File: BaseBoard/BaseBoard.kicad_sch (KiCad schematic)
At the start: 22 parts, among them J1 OHIS RJ45, J2 Radio Board, J3 Dynamic/Electret, J6 Speaker Input Config

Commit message: Happy with BaseBoard and Icom-RJ45. Working on Icom-GX16 #1
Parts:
- added G2: Board_Artwork, OHIS:Logo_OHIS_Medium, symbol Smitty:Board_Artwork
- G1: footprint OHIS:Logo_OHIS_Small -> OHIS:Logo_OHIS_Medium
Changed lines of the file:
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@@
+	)
+	(symbol
+		(lib_id "Smitty:Board_Artwork")
+		(at 83.82 168.91 0)
+		(unit 1)
+		(exclude_from_sim no)
+		(in_bom no)
+		(on_board yes)
+		(dnp no)
+		(fields_autoplaced yes)
+		(property "Reference" "G2"
+			(at 87.63 169.4179 0)
+			(effects
+				(font
+					(size 1.27 1.27)
+				)
+				(justify left)
+			)
+		)
+		(property "Value" "Board_Artwork"
+			(at 87.63 171.9579 0)
+			(effects
+				(font
+					(size 1.27 1.27)
+				)
+				(justify left)
+			)
+		)
+		(property "Footprint" "OHIS:Logo_OHIS_Medium"
+			(at 83.82 168.91 0)
+			(effects
+				(font
+					(size 1.27 1.27)
+				)
+			)
+		)
+		(property "Datasheet" ""
+			(at 83.82 168.91 0)
+			(effects
+				(font
+					(size 1.27 1.27)
+				)
+				(hide yes)
+			)
+		)
+		(property "Description" ""
+			(at 83.82 168.91 0)
+			(effects
+				(font
+					(size 1.27 1.27)
+				)
+				(hide yes)
+			)
+		)
+		(instances
+			(project "BaseBoard"
+				(path "/6a3924fa-c381-477c-bc5e-4effe098c460"
+					(reference "G2")
+					(unit 1)
+				)
+			)
+		)
 	)
 	(symbol
@@
 			)
 		)
-		(property "Footprint" "OHIS:Logo_OHIS_Small"
+		(property "Footprint" "OHIS:Logo_OHIS_Medium"
 			(at 83.82 161.29 0)
 			(effects

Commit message: Updated BOM parts, among other things. Sorry, it's been a while. #1
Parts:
- removed RV1: 1k, Potentiometer_THT:Potentiometer_Piher_PT-6-H_Horizontal, symbol Device:R_Potentiometer
- added BOM1, BOM13, BOM17, BOM9: M3 6mm SS screw, Libraries:BOM_Item, symbol smitty:BOM_Item
- added BOM10, BOM14, BOM18, BOM3: M3 14mm brass standoff, Libraries:BOM_Item, symbol smitty:BOM_Item
- added BOM11, BOM15, BOM19, BOM7: M3 3mm ABS standoff, Libraries:BOM_Item, symbol smitty:BOM_Item
- added BOM12, BOM16, BOM6, BOM8: M3 10mm SS screw, Libraries:BOM_Item, symbol smitty:BOM_Item
- added BOM2: Top Board, Libraries:BOM_Item, symbol smitty:BOM_Item
- added BOM20, BOM21, BOM22, BOM23, BOM24: .1" Jumper, Libraries:BOM_Item, symbol smitty:BOM_Item
- added BOM4: Main Board, Libraries:BOM_Item, symbol smitty:BOM_Item
- added BOM5: Bottom Board, Libraries:BOM_Item, symbol smitty:BOM_Item
- added RV2: 1k, Potentiometer_THT:Potentiometer_Piher_PT-6-H_Horizontal, symbol Device:R_Potentiometer_Small
- C1, C2: Link (none) -> https://www.mouser.com/ProductDetail/TDK/FG28X5R1E106MRT06?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; Manufacturer (none) -> TDK; Part Number (none) -> FG28X5R1E106MRT06; Z0 Buy in Qty (none) -> 200; Z1 Cost to buy (none) -> =32.40
- C3, C4, R11, R12, R5, R7: now not fitted; now left out of the parts list
- J1: Link (none) -> https://www.mouser.com/ProductDetail/523-RJHSE-5380; Manufacturer (none) -> Amphenol; Part Number (none) -> RJHSE-5381; Z0 Buy in Qty (none) -> 120; Z1 Cost to buy (none) -> =127.20; Z2 Cost per part (none) -> =IFERROR(OFFSET(INDIRECT(CELL("Address")), 0, -1)/OFFSET(IN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; Z3 Cost per Qty (none) -> =OFFSET(INDIRECT(CELL("Address")), 0, -1)*INDIRECT(ADDRESS(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
- J3, J6: Link (none) -> https://www.ebay.com/itm/181918596973; Manufacturer (none) -> Generic; Part Number (none) -> .1" 3x40 right angle 2.54mm Pin Header; Z0 Buy in Qty (none) -> 40; Z1 Cost to buy (none) -> 2.49; Z2 Cost per part (none) -> =IFERROR(OFFSET(INDIRECT(CELL("Address")), 0, -1)/OFFSET(IN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; Z3 Cost per Qty (none) -> =OFFSET(INDIRECT(CELL("Address")), 0, -1)*INDIRECT(ADDRESS(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
- R1: Link (none) -> https://www.mouser.com/ProductDetail/YAGEO/CFR-12JB-52-1K?q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; Manufacturer (none) -> YAGEO; Part Number (none) -> CFR-12JB-52-1K; Z0 Buy in Qty (none) -> 100; Z1 Cost to buy (none) -> 2.80; Z2 Cost per part (none) -> =IFERROR(OFFSET(INDIRECT(CELL("Address")), 0, -1)/OFFSET(IN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; Z3 Cost per Qty (none) -> =OFFSET(INDIRECT(CELL("Address")), 0, -1)*INDIRECT(ADDRESS(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
- R4: Link (none) -> https://www.mouser.com/ProductDetail/YAGEO/CFR-12JB-52-6K2?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; Manufacturer (none) -> YAGEO; Part Number (none) -> CFR-12JB-52-6K2; Z0 Buy in Qty (none) -> 100; Z1 Cost to buy (none) -> 1.90
- R6, R8: Link (none) -> https://www.mouser.com/ProductDetail/YAGEO/CFR-12JB-52-100R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; Manufacturer (none) -> YAGEO; Part Number (none) -> CFR-12JB-52-100R; Z0 Buy in Qty (none) -> 100; Z1 Cost to buy (none) -> 2.80; Z2 Cost per part (none) -> =IFERROR(OFFSET(INDIRECT(CELL("Address")), 0, -1)/OFFSET(IN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; Z3 Cost per Qty (none) -> =OFFSET(INDIRECT(CELL("Address")), 0, -1)*INDIRECT(ADDRESS(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
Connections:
- net Radio Mic Gnd: now also RV2.1
- net at C2.1, C4.1: now also RV2.2
- net at C1.1, C3.1: now also RV2.3
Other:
- note added: "BOM: 1x 5381 RF45 with LEDs 1x 2x2 pin header right angle 1x 2x4 pin header right angle 2x 10uF 1x 6.2k resistor 1x 1k resistor 2x 100R resistors 1x 1k potentiometer"
- moved on the sheet: G1, G2

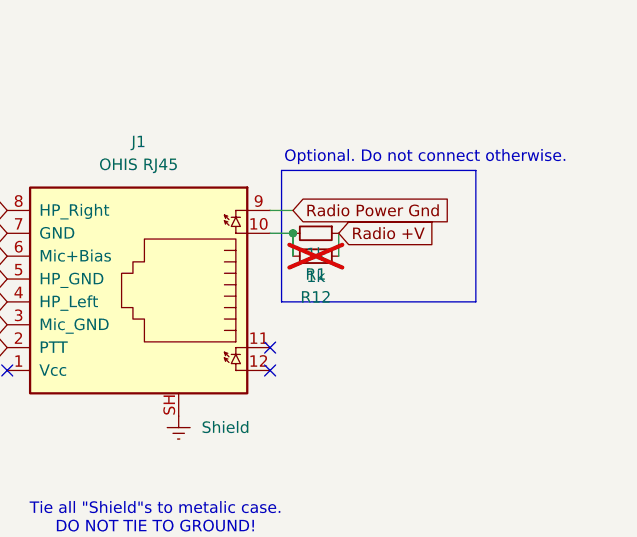
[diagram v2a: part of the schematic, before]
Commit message: Added an Interactive BOM for the Base Board assembly.
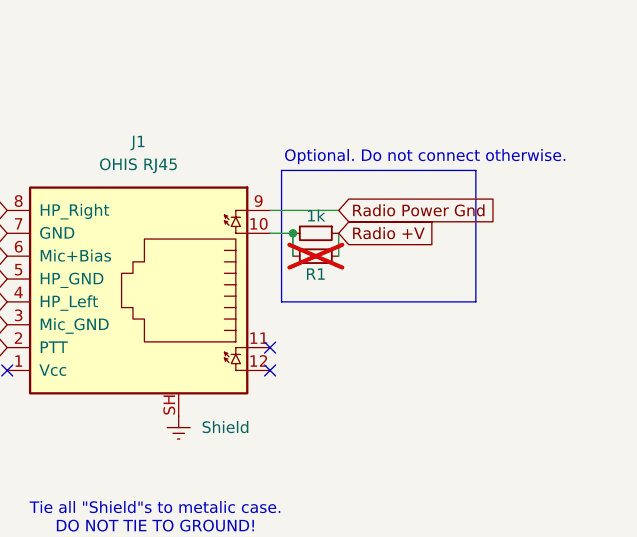
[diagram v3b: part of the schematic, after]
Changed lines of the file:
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@@
 (kicad_sch
-	(version 20231120)
+	(version 20250114)
 	(generator "eeschema")
-	(generator_version "8.0")
+	(generator_version "9.0")
 	(paper "A4")
+	(rectangle
+		(start 242.57 34.925)
+		(end 264.16 49.53)
+		(stroke
+			(width 0)
+			(type default)
+		)
+		(fill
+			(type none)
+		)
+	)
+	(text "Stereo Source"
+		(exclude_from_sim no)
+		(at 148.082 97.79 0)
+		(effects
+			(font
+				(size 1.27 1.27)
+			)
+		)
+	)
+	(text "OHIS Side: Electret Mic\nBias voltage."
+		(exclude_from_sim no)
+		(at 151.638 26.67 0)
+		(effects
+			(font
+				(size 1.27 1.27)
+			)
+		)
+	)
+	(text "Mono Source"
+		(exclude_from_sim no)
+		(at 147.574 100.33 0)
+		(effects
+			(font
+				(size 1.27 1.27)
+			)
+		)
+	)
+	(text "Radio Side: Dynamic Mic.\n20dB pad, DC block."
+		(exclude_from_sim no)
+		(at 122.682 33.274 0)
+		(effects
+			(font
+				(size 1.27 1.27)
+			)
+		)
+	)
+	(text "Tie all \"Shield\"s to metalic case.\nDO NOT TIE TO GROUND!"
+		(exclude_from_sim no)
+		(at 228.6 73.66 0)
+		(effects
+			(font
+				(size 1.27 1.27)
+			)
+		)
+	)
+	(text "1k*10uF=16Hz\n600*10uF=26Hz"
+		(exclude_from_sim no)
+		(at 131.572 20.574 0)
+		(effects
+			(font
+				(size 1.27 1.27)
+			)
+		)
+	)
+	(text "BOM:\n1x 5381 RF45 with LEDs\n1x 2x2 pin header right angle\n1x 2x4 pin header right angle\n2x 10uF\n1x 6.2k resistor\n1x 1k resistor\n2x 100R resistors\n1x 1k potentiometer\n"
+		(exclude_from_sim no)
+		(at 44.45 35.56 0)
+		(effects
+			(font
+				(size 1.27 1.27)
+			)
+			(justify left)
+		)
+	)
+	(text "Jumper: Headphone\nNo Jumper: Speaker"
+		(exclude_from_sim no)
+		(at 151.13 104.394 0)
+		(effects
+			(font
+				(size 1.27 1.27)
+			)
+		)
+	)
+	(text "Optional. Do not connect otherwise."
+		(exclude_from_sim no)
+		(at 258.572 33.528 0)
+		(effects
+			(font
+				(size 1.27 1.27)
+			)
+		)
+	)
 	(junction
 		(at 116.84 44.45)
@@
 	(wire
 		(pts
-			(xy 243.84 39.37) (xy 241.3 39.37)
+			(xy 248.92 39.37) (xy 241.3 39.37)
 		)
 		(stroke
@@
 		)
 	)
-	(rectangle
-		(start 242.57 34.925)
-		(end 264.16 49.53)
-		(stroke
-			(width 0)
-			(type default)
-		)
-		(fill
-			(type none)
-		)
-	)
-	(text "Stereo Source"
-		(exclude_from_sim no)
-		(at 148.082 97.79 0)
-		(effects
-			(font
-				(size 1.27 1.27)
-			)
-		)
-	)
-	(text "OHIS Side: Electret Mic\nBias voltage."
-		(exclude_from_sim no)
-		(at 151.638 26.67 0)
-		(effects
-			(font
-				(size 1.27 1.27)
-			)
-		)
-	)
-	(text "Mono Source"
-		(exclude_from_sim no)
-		(at 147.574 100.33 0)
-		(effects
-			(font
-				(size 1.27 1.27)
-			)
-		)
-	)
-	(text "Radio Side: Dynamic Mic.\n20dB pad, DC block."
-		(exclude_from_sim no)
-		(at 122.682 33.274 0)
-		(effects
-			(font
-				(size 1.27 1.27)
-			)
-		)
-	)
-	(text "Tie all \"Shield\"s to metalic case.\nDO NOT TIE TO GROUND!"
-		(exclude_from_sim no)
-		(at 228.6 73.66 0)
-		(effects
-			(font
-				(size 1.27 1.27)
-			)
-		)
-	)
-	(text "1k*10uF=16Hz\n600*10uF=26Hz"
-		(exclude_from_sim no)
-		(at 131.572 20.574 0)
-		(effects
-			(font
-				(size 1.27 1.27)
-			)
-		)
-	)
-	(text "BOM:\n1x 5381 RF45 with LEDs\n1x 2x2 pin header right angle\n1x 2x4 pin header right angle\n2x 10uF\n1x 6.2k resistor\n1x 1k resistor\n2x 100R resistors\n1x 1k potentiometer\n"
-		(exclude_from_sim no)
-		(at 44.45 35.56 0)
-		(effects
-			(font
-				(size 1.27 1.27)
-			)
-			(justify left)
-		)
-	)
-	(text "Jumper: Headphone\nNo Jumper: Speaker"
-		(exclude_from_sim no)
-		(at 151.13 104.394 0)
-		(effects
-			(font
-				(size 1.27 1.27)
-			)
-		)
-	)
-	(text "Optional. Do not connect otherwise."
-		(exclude_from_sim no)
-		(at 258.572 33.528 0)
-		(effects
-			(font
-				(size 1.27 1.27)
-			)
-		)
-	)
 	(global_label "Radio Mic Gnd"
 		(shape input)
@@
 	(global_label "Radio Power Gnd"
 		(shape input)
-		(at 243.84 39.37 0)
+		(at 248.92 39.37 0)
 		(fields_autoplaced yes)
 		(effects
@@
 		)
 		(property "Intersheetrefs" "${INTERSHEET_REFS}"
-			(at 263.2745 39.37 0)
+			(at 268.3545 39.37 0)
 			(effects
 				(font
@@
 					(size 1.27 1.27)
 				)
+				(hide yes)
 			)
 		)
@@
 					(size 1.27 1.27)
 				)
+				(hide yes)
 			)
 		)
@@
 		)
 		(property "Value" "1k"
-			(at 246.38 44.196 90)
+			(at 246.38 40.005 90)
 			(effects
 				(font
@@
 		)
 	)
+	(embedded_fonts no)
 )
